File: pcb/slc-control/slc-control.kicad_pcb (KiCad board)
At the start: 2 copper layers, 100 x 45 mm, 89 parts, among them J1 USB_C_Receptacle_USB2.0_16P, J2 Conn_01x02_Socket, J3 Conn_01x02_Socket, J4 Conn_01x02_Socket, J5 Conn_01x02_Socket, J6 Conn_01x05_Socket, J7 Conn_ARM_SWD_TagConnect_TC203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, J8 Conn_01x07_Pin, Q1 AO3400A, Q2 AO3401A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

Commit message: Final pcb
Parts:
- removed Q1: AO3400A, Package_TO_SOT_SMD:SOT-23
- removed Q2: AO3401A, Package_TO_SOT_SMD:SOT-23
- removed R3: 10k, Resistor_SMD:R_0402_1005Metric
- added BT1: CR1220, User_Footprints:CR1220, F.Cu at (76.6, 69.2)
- added C28: 47p, Capacitor_SMD:C_0402_1005Metric, F.Cu at (106.8, 69.0)
- added C29: 10u, Capacitor_SMD:C_0603_1608Metric, F.Cu at (85.6, 68.2)
- added C30: 100n, Capacitor_SMD:C_0402_1005Metric, F.Cu at (87.0, 67.8)
- added C31: 100n, Capacitor_SMD:C_0402_1005Metric, F.Cu at (87.0, 64.8)
- added D5: SD103AWS, Diode_SMD:D_SOD-323, F.Cu at (85.4, 64.8)
- added L2: 47n, Inductor_SMD:L_0603_1608Metric, F.Cu at (109.2, 68.2)
- added R24: 22, Resistor_SMD:R_0402_1005Metric, F.Cu at (107.0, 65.2)
- added U8: GPS02-UBX, User_Footprints:GPS02-UBX, F.Cu at (96.4, 63.6)
- J6: value Conn_01x05_Socket -> Conn_Coaxial; footprint Connector_PinHeader_2.54mm:PinHeader_1x05_P2.54mm_Vertical -> User_Footprints:BWSMA-KWE-Z001
- moved D2 145.0 mm to (39.2, 97.3)
- moved D3 145.0 mm to (39.2, 84.1)
- moved Q6 145.0 mm to (45.7, 97.5)
- moved Q7 145.0 mm to (39.4, 91.8)
- moved Q8 145.0 mm to (45.7, 84.3)
- moved Q9 145.0 mm to (39.4, 78.6)
- moved R13 145.0 mm to (45.1, 89.5)
- moved R14 145.0 mm to (45.1, 76.3)
- moved C8 138.0 mm to (38.8, 58.6), turned to 90 degrees
- moved C9 137.7 mm to (36.4, 58.6), turned to 90 degrees
- moved C11 136.9 mm to (36.4, 64.4), turned to -90 degrees
- moved C1 130.9 mm to (37.6, 71.8), turned to 90 degrees
- moved D1 129.9 mm to (45.6, 67.0), turned to 90 degrees
- moved C3 129.3 mm to (40.0, 71.8), turned to 90 degrees
- moved U1 126.1 mm to (41.6, 65.7), turned to -90 degrees
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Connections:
- J4 pad 1: /SNS1 -> /SNS2
- J4 pad 2: /SNS2 -> /SNS1
- J5 pad 1: /SNS3 -> Net-(J5-Pin_1)
- J5 pad 2: Net-(J5-Pin_2) -> /SNS3
- J6 pad 1: Net-(J6-Pin_1) -> /ANT
- JP1 pad 2: Net-(J5-Pin_2) -> Net-(J5-Pin_1)
- U7 pad 33: unconnected-(U7-PA11-Pad33) -> /USB-
- U7 pad 34: unconnected-(U7-PA12-Pad34) -> /USB+
- U7 pad 37: unconnected-(U7-PA13-Pad37) -> /SWDIO
- U7 pad 38: unconnected-(U7-PA14-Pad38) -> /SWCLK
- U7 pad 40: unconnected-(U7-PB3-Pad40) -> /SWO
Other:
- board size 100 x 45 mm -> 99 x 45 mm
- copper layers 2 -> 4

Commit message: Finish layout
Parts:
- removed JP1: SolderJumper_3_Open, Jumper:SolderJumper-3_P1.3mm_Open_RoundedPad1.0x1.5mm
- removed R11: 10k, Resistor_SMD:R_0402_1005Metric
- added C32: 2u2, Capacitor_SMD:C_0402_1005Metric, F.Cu at (107.2, 126.4)
- added C33: 100n, Capacitor_SMD:C_0402_1005Metric, F.Cu at (110.5, 124.3)
- added C34: 100n, Capacitor_SMD:C_0402_1005Metric, F.Cu at (108.2, 126.4)
- added C35: 2u2, Capacitor_SMD:C_0402_1005Metric, F.Cu at (96.9, 114.1)
- added C36: 100n, Capacitor_SMD:C_0402_1005Metric, F.Cu at (85.9, 118.1)
- added R3: 33k, Resistor_SMD:R_0402_1005Metric, F.Cu at (105.3, 101.5)
- added U9: ICM-42688-P, Package_LGA:LGA-14_3x2.5mm_P0.5mm_LayoutBorder3x4y, F.Cu at (110.5, 126.4)
- moved C15 73.4 mm to (118.4, 126.6), turned to 90 degrees
- moved C14 73.4 mm to (117.4, 126.6), turned to 90 degrees
- moved U6 72.7 mm to (120.3, 126.6), turned to 90 degrees
- moved R21 61.2 mm to (148.1, 122.6), turned to 90 degrees
- moved C12 59.8 mm to (100.1, 113.3)
- moved Q9 58.6 mm to (71.6, 127.6), turned to 180 degrees
- moved D3 57.9 mm to (71.4, 132.3), turned to 180 degrees
- moved R14 57.8 mm to (75.9, 125.2), turned to -90 degrees
- moved R18 57.0 mm to (148.1, 117.3), turned to -90 degrees
- moved R12 55.7 mm to (144.8, 126.4), turned to 90 degrees
- moved R2 54.8 mm to (91.7, 105.7), turned to 0 degrees
- moved R22 54.4 mm to (143.9, 120.8), turned to 90 degrees
- moved Q4 54.2 mm to (147.3, 126.8)
- moved Q8 54.1 mm to (77.2, 128.2), turned to 90 degrees
- moved C8 53.7 mm to (72.2, 100.6)
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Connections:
- C18 pad 2: /XTALO -> /XTALI
- C23 pad 1: /RST -> /RES
- C25 pad 1: +3VA3 -> +3V3A
- C26 pad 1: +3VA3 -> +3V3A
- FB1 pad 1: +3VA3 -> +3V3A
- J5 pad 1: Net-(J5-Pin_1) -> /REP
- J8 pad 3: /SCK -> /SDK
- J8 pad 4: /MOSI -> /SDI
- R10 pad 2: /XTALI -> /XTALO
- U7 pad 10: unconnected-(U7-PA2-Pad10) -> /CSP
- U7 pad 11: unconnected-(U7-PA3-Pad11) -> /SIG1
- U7 pad 12: unconnected-(U7-PA4-Pad12) -> /CSG
- U7 pad 13: unconnected-(U7-PA5-Pad13) -> /SCK
- U7 pad 14: unconnected-(U7-PA6-Pad14) -> /MISO
- U7 pad 15: unconnected-(U7-PA7-Pad15) -> /MOSI
- U7 pad 16: unconnected-(U7-PB0-Pad16) -> /INTG1
- U7 pad 17: unconnected-(U7-PB1-Pad17) -> /PPS
- U7 pad 18: unconnected-(U7-PB2-Pad18) -> /DRDYP
- U7 pad 2: unconnected-(U7-PC13-Pad2) -> /BTN3
- U7 pad 20: +3V3 -> +3V3A
- U7 pad 21: +3VA3 -> +3V3A
- U7 pad 22: unconnected-(U7-PB10-Pad22) -> /GTX
- U7 pad 25: unconnected-(U7-PB11-Pad25) -> /GRX
- U7 pad 26: unconnected-(U7-PB12-Pad26) -> /DC
- U7 pad 27: unconnected-(U7-PB13-Pad27) -> /SDK
- U7 pad 28: unconnected-(U7-PB14-Pad28) -> /CSD
- U7 pad 29: unconnected-(U7-PB15-Pad29) -> /SDI
- U7 pad 3: unconnected-(U7-PC14-Pad3) -> /BTN2
- U7 pad 30: unconnected-(U7-PA8-Pad30) -> /SDAM
- U7 pad 31: unconnected-(U7-PA9-Pad31) -> /SCLM
- U7 pad 32: unconnected-(U7-PA10-Pad32) -> /DRDYM
- U7 pad 39: unconnected-(U7-PA15-Pad39) -> /SCLE
- U7 pad 4: unconnected-(U7-PC15-Pad4) -> /BTN1
- U7 pad 41: unconnected-(U7-PB4-Pad41) -> /DRV1
- U7 pad 42: unconnected-(U7-PB5-Pad42) -> /DRV2
- U7 pad 43: unconnected-(U7-PB6-Pad43) -> /REPH
- U7 pad 44: unconnected-(U7-PB7-Pad44) -> /SDAE
- U7 pad 45: /BOOT0 -> /BTN4
- U7 pad 46: unconnected-(U7-PB9-Pad46) -> /REPL
- U7 pad 8: unconnected-(U7-PA0-Pad8) -> /SIG3
- U7 pad 9: unconnected-(U7-PA1-Pad9) -> /SIG2
- U8 pad 18: /GRST -> +3V3
- Y1 pad 1: /XTALO -> /XTALI
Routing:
- net +12V: track 0.00 -> 180.8 mm, vias 0 -> 5
- net GND: track 0.00 -> 176.4 mm, vias 0 -> 86
- net /BTN1: track 0.00 -> 95.0 mm, vias 0 -> 1
- net /BTN4: track 0.00 -> 91.6 mm, vias 0 -> 1
- net /BTN2: track 0.00 -> 88.8 mm, vias 0 -> 1
- net /REPH: track 0.00 -> 85.9 mm
- net /REPL: track 0.00 -> 83.9 mm
- net /BTN3: track 0.00 -> 83.4 mm, vias 0 -> 1
- net +5V: track 0.00 -> 74.5 mm, vias 0 -> 6
- net +3V3: track 0.00 -> 65.7 mm, vias 0 -> 32
- net /SIG3: track 0.00 -> 64.4 mm
- net /SIG1: track 0.00 -> 63.5 mm
- net /SIG2: track 0.00 -> 63.1 mm
- net /PPS: track 0.00 -> 44.7 mm, vias 0 -> 2
- net /GRX: track 0.00 -> 42.0 mm, vias 0 -> 2
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- added copper zone on In2.Cu, net +3V3
- added copper zone on F.Cu, net /OUT1
- added copper zone on F.Cu, net /OUT2
- added copper zone on B.Cu, net GND
- added copper zone on F.Cu, net GND
- added copper zone on In1.Cu, net GND

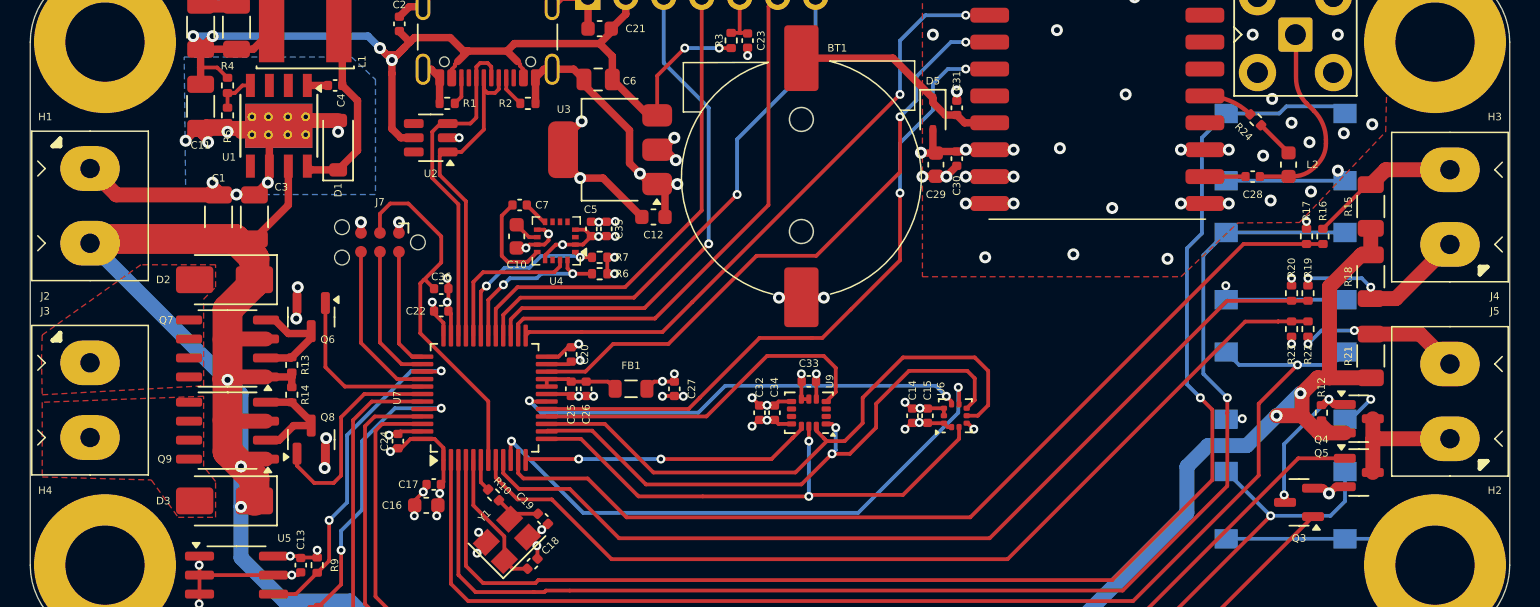
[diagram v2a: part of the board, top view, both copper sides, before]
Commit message: Change extended parts to do not place
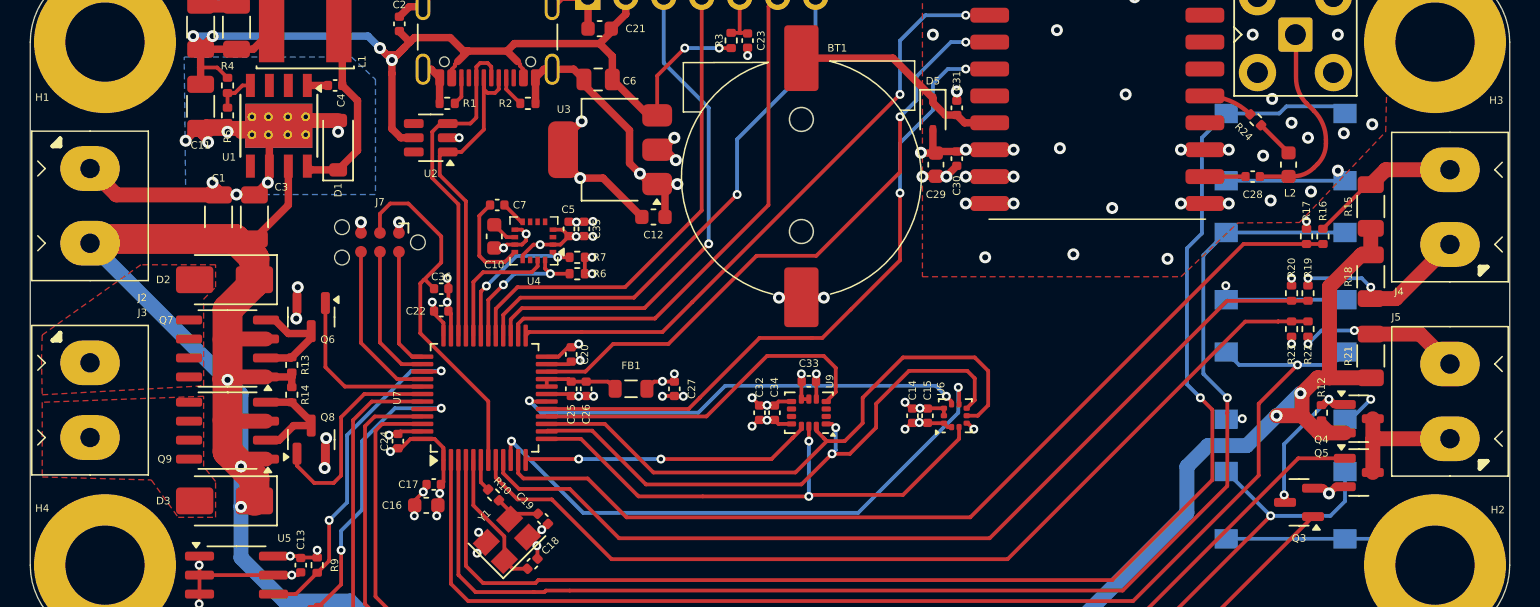
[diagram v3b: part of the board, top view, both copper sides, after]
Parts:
- moved C10 1.50 mm to (89.4, 114.6)
- moved C35 1.50 mm to (95.4, 114.1)
- moved C5 1.50 mm to (94.4, 114.1)
- moved C7 1.50 mm to (89.6, 112.5)
- moved R6 1.50 mm to (95.0, 117.1)
- moved R7 1.50 mm to (95.0, 116.0)
- moved U4 1.50 mm to (92.1, 114.9)
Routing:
- net /SCLM: track 11.9 -> 10.4 mm
- net /SDAM: track 11.1 -> 9.62 mm
- net /DRDYM: track 10.2 -> 8.75 mm

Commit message: Final production
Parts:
- moved R13 1.20 mm to (77.1, 123.2)
- moved R14 1.20 mm to (77.1, 125.2)
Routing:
- net +12V: track 180.8 -> 181.9 mm
- net /Output1/PDRV: track 7.50 -> 8.20 mm
- net /Output2/PDRV: track 7.25 -> 7.95 mm
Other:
- board text added: "12V"
- board text added: "GND"
- board text added: "OUT1"
- board text added: "OUT2"
- board text added: "REP"
- board text added: "SNS1"
- board text added: "SNS2"
- board text added: "SNS3"

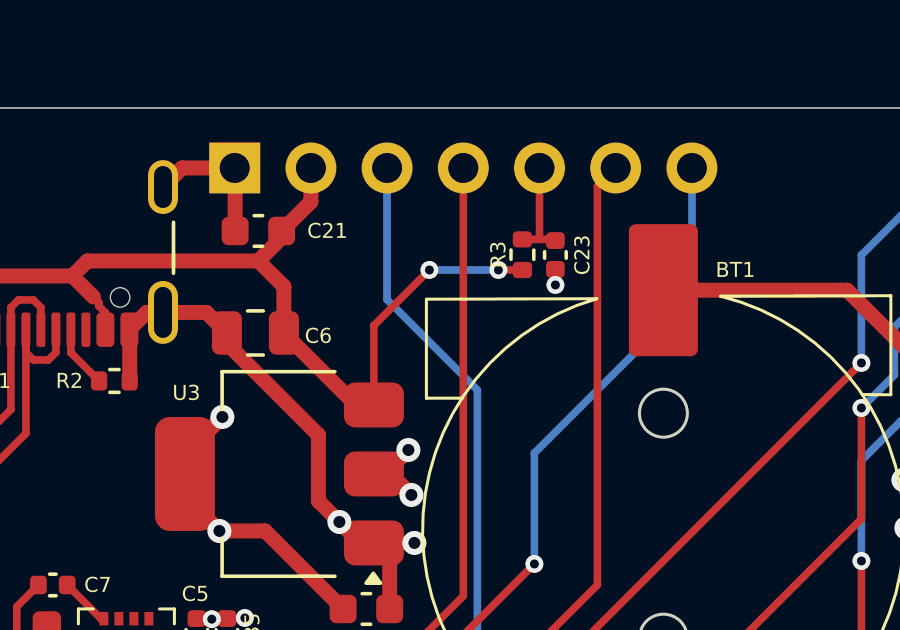
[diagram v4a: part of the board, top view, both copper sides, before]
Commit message: Fix ssd1309 reset input voltage
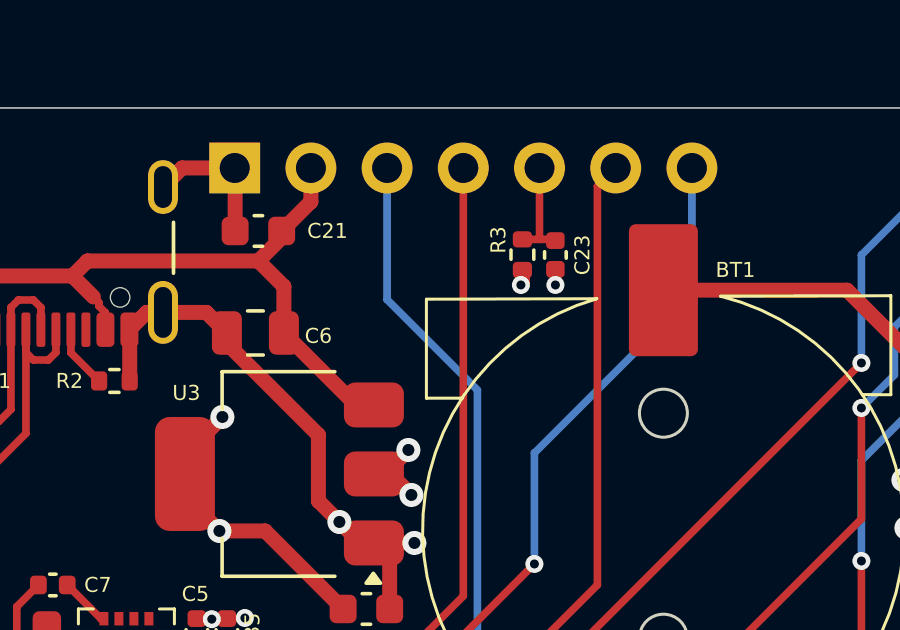
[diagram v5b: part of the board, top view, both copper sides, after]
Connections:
- R3 pad 1: +5V -> +3V3
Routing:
- net +5V: track 74.5 -> 66.2 mm, vias 6 -> 4
- net +3V3: track 65.7 -> 66.2 mm, vias 32 -> 33
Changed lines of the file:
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@@
 		(tags "resistor")
 		(property "Reference" "R3"
-			(at 0 -0.8 90)
+			(at 0.490001 -0.8 90)
 			(layer "F.SilkS")
 			(effects
@@
 			(layers "F.Cu" "F.Paste" "F.Mask")
 			(roundrect_rratio 0.25)
-			(net 5 "+5V")
+			(net 2 "+3V3")
 			(pintype "passive")
 		)
@@
 	)
 	(segment
+		(start 105.3 102)
+		(end 105.3 102.45)
+		(width 0.5)
+		(layer "F.Cu")
+		(net 2)
+	)
+	(segment
 		(start 108.2 125.92)
 		(end 107.72 125.92)
@@
 	)
 	(segment
+		(start 105.3 102.45)
+		(end 105.25 102.5)
+		(width 0.5)
+		(layer "F.Cu")
+		(net 2)
+	)
+	(segment
 		(start 100.9 108.8)
 		(end 101.6 109.5)
@@
 	)
 	(via
+		(at 105.25 102.5)
+		(size 0.6)
+		(drill 0.3)
+		(layers "F.Cu" "B.Cu")
+		(net 2)
+	)
+	(via
 		(at 85.8 131.8)
 		(size 0.6)
@@
 	)
 	(segment
-		(start 105.3 102)
-		(end 104.5 102)
-		(width 0.254)
-		(layer "F.Cu")
-		(net 5)
-	)
-	(segment
 		(start 69.8 101.7)
 		(end 69.3 101.2)
@@
 	)
 	(segment
-		(start 100.35 103.85)
-		(end 102.2 102)
-		(width 0.254)
-		(layer "F.Cu")
-		(net 5)
-	)
-	(segment
 		(start 81.8 102)
 		(end 82.25 102.45)
@@
 	)
 	(segment
-		(start 100.35 106.5)
-		(end 100.35 103.85)
-		(width 0.254)
-		(layer "F.Cu")
-		(net 5)
-	)
-	(segment
 		(start 86.6 103.99)
 		(end 86.6 103.423435)
@@
 	)
 	(via
-		(at 104.5 102)
-		(size 0.6)
-		(drill 0.3)
-		(layers "F.Cu" "B.Cu")
-		(net 5)
-	)
-	(via
 		(at 69.3 101.2)
 		(size 0.8)
@@
 		(net 5)
 	)
-	(via
-		(at 102.2 102)
-		(size 0.6)
-		(drill 0.3)
-		(layers "F.Cu" "B.Cu")
-		(net 5)
-	)
 	(segment
 		(start 81 101.2)
@@
 	)
 	(segment
-		(start 104.5 102)
-		(end 102.2 102)
-		(width 0.254)
-		(layer "B.Cu")
-		(net 5)
-	)
-	(segment
 		(start 81.8 102)
 		(end 81 101.2)
@@
 	)
 	(zone
-		(net 79)
-		(net_name "Net-(L2-Pad1)")
+		(net 78)
+		(net_name "Net-(U8-ANT)")
 		(layer "F.Cu")
 		(name "$teardrop_padvia$")
 		(hatch full 0.1)
-		(priority 30008)
+		(priority 30004)
 		(attr
 			(teardrop
@@
 		(polygon
 			(pts
-				(xy 141.24676 107.438163) (xy 141.221296 107.392751) (xy 141.195833 107.33999) (xy 141.17037 107.279878)
-				(xy 141.144907 107.212417) (xy 141.119444 107.137606) (xy 140.759917 107.159917) (xy 140.737606 107.519444)
-				(xy 140.797717 107.530207) (xy 140.857828 107.54832) (xy 140.91794 107.573783) (xy 140.978051 107.606596)
-				(xy 141.038163 107.64676)
+				(xy 139.16 110.7475) (xy 139.227495 110.7581) (xy 139.29499 110.77665) (xy 139.362484 110.803149)
+				(xy 139.429979 110.837599) (xy 139.497475 110.88) (xy 139.721 110.6) (xy 139.497475 110.32) (xy 139.429979 110.3624)
+				(xy 139.362484 110.39685) (xy 139.29499 110.423349) (xy 139.227495 110.441899) (xy 139.16 110.4525)
 			)
 		)
@@
 		(name "$teardrop_padvia$")
 		(hatch full 0.1)
-		(priority 30000)
+		(priority 30001)
 		(attr
 			(teardrop
@@
 	)
 	(zone
-		(net 78)
-		(net_name "Net-(U8-ANT)")
+		(net 79)
+		(net_name "Net-(L2-Pad1)")
 		(layer "F.Cu")
 		(name "$teardrop_padvia$")
@@
 		(polygon
 			(pts
-				(xy 139.16 110.7475) (xy 139.227495 110.7581) (xy 139.29499 110.77665) (xy 139.362484 110.803149)
-				(xy 139.429979 110.837599) (xy 139.497475 110.88) (xy 139.721 110.6) (xy 139.497475 110.32) (xy 139.429979 110.3624)
-				(xy 139.362484 110.39685) (xy 139.29499 110.423349) (xy 139.227495 110.441899) (xy 139.16 110.4525)
-			)
-		)
-	)
-	(zone
-		(net 76)
-		(net_name "/ANT")
-		(layer "F.Cu")
-		(name "$teardrop_padvia$")
-		(hatch full 0.1)
-		(priority 30007)
-		(attr
-			(teardrop
-				(type padvia)
-			)
-		)
-		(connect_pads yes
-			(clearance 0)
-		)
-		(min_thickness 0.0254)
-		(filled_areas_thickness no)
-		(fill yes
-			(thermal_gap 0.5)
-			(thermal_bridge_width 0.5)
-			(island_removal_mode 1)
-			(island_area_min 10)
-		)
-		(polygon
-			(pts
-				(xy 141.24 110.4525) (xy 141.172504 110.441899) (xy 141.105009 110.423349) (xy 141.037515 110.39685)
-				(xy 140.97002 110.3624) (xy 140.902525 110.32) (xy 140.679 110.6) (xy 140.902525 110.88) (xy 140.97002 110.837599)
-				(xy 141.037515 110.803149) (xy 141.105009 110.77665) (xy 141.172504 110.7581) (xy 141.24 110.7475)
+				(xy 141.24676 107.438163) (xy 141.221296 107.392751) (xy 141.195833 107.33999) (xy 141.17037 107.279878)
+				(xy 141.144907 107.212417) (xy 141.119444 107.137606) (xy 140.759917 107.159917) (xy 140.737606 107.519444)
+				(xy 140.797717 107.530207) (xy 140.857828 107.54832) (xy 140.91794 107.573783) (xy 140.978051 107.606596)
+				(xy 141.038163 107.64676)
 			)
 		)
@@
 		(name "$teardrop_padvia$")
 		(hatch full 0.1)
-		(priority 30001)
+		(priority 30002)
 		(attr
 			(teardrop
@@
 		(name "$teardrop_padvia$")
 		(hatch full 0.1)
-		(priority 30002)
+		(priority 30003)
 		(attr
 			(teardrop
@@
 	)
 	(zone
-		(net 80)
-		(net_name "Net-(U8-VCC_RF)")
+		(net 76)
+		(net_name "/ANT")
 		(layer "F.Cu")
 		(name "$teardrop_padvia$")
 		(hatch full 0.1)
-		(priority 30009)
+		(priority 30005)
 		(attr
 			(teardrop
@@
 		(polygon
 			(pts
-				(xy 139.636842 106.276555) (xy 139.64526 106.304626) (xy 139.653678 106.338897) (xy 139.662097 106.379369)
-				(xy 139.670515 106.426042) (xy 139.678934 106.478916) (xy 140.040149 106.44001) (xy 140.046971 106.083623)
-				(xy 140.002374 106.090145) (xy 139.957777 106.089895) (xy 139.913179 106.082874) (xy 139.868582 106.06908)
-				(xy 139.823986 106.048516)
+				(xy 141.24 110.4525) (xy 141.172504 110.441899) (xy 141.105009 110.423349) (xy 141.037515 110.39685)
+				(xy 140.97002 110.3624) (xy 140.902525 110.32) (xy 140.679 110.6) (xy 140.902525 110.88) (xy 140.97002 110.837599)
+				(xy 141.037515 110.803149) (xy 141.105009 110.77665) (xy 141.172504 110.7581) (xy 141.24 110.7475)
 			)
 		)
@@
 			)
 		)
+	)
+	(zone
+		(net 80)
+		(net_name "Net-(U8-VCC_RF)")
+		(layer "F.Cu")
+		(name "$teardrop_padvia$")
+		(hatch full 0.1)
+		(priority 30007)
+		(attr
+			(teardrop
+				(type padvia)
+			)
+		)
+		(connect_pads yes
+			(clearance 0)
+		)
+		(min_thickness 0.0254)
+		(filled_areas_thickness no)
+		(fill yes
+			(thermal_gap 0.5)
+			(thermal_bridge_width 0.5)
+			(island_removal_mode 1)
+			(island_area_min 10)
+		)
+		(polygon
+			(pts
+				(xy 139.636842 106.276555) (xy 139.64526 106.304626) (xy 139.653678 106.338897) (xy 139.662097 106.379369)
+				(xy 139.670515 106.426042) (xy 139.678934 106.478916) (xy 140.040149 106.44001) (xy 140.046971 106.083623)
+				(xy 140.002374 106.090145) (xy 139.957777 106.089895) (xy 139.913179 106.082874) (xy 139.868582 106.06908)
+				(xy 139.823986 106.048516)
+			)
+		)
